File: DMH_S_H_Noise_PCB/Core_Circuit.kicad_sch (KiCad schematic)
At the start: 61 parts, among them Q1 BC548, Q2 MMBFJ113, Q3 BC548, SW1 SW_Push, U1 TL074, U2 TL072, U3 TL074

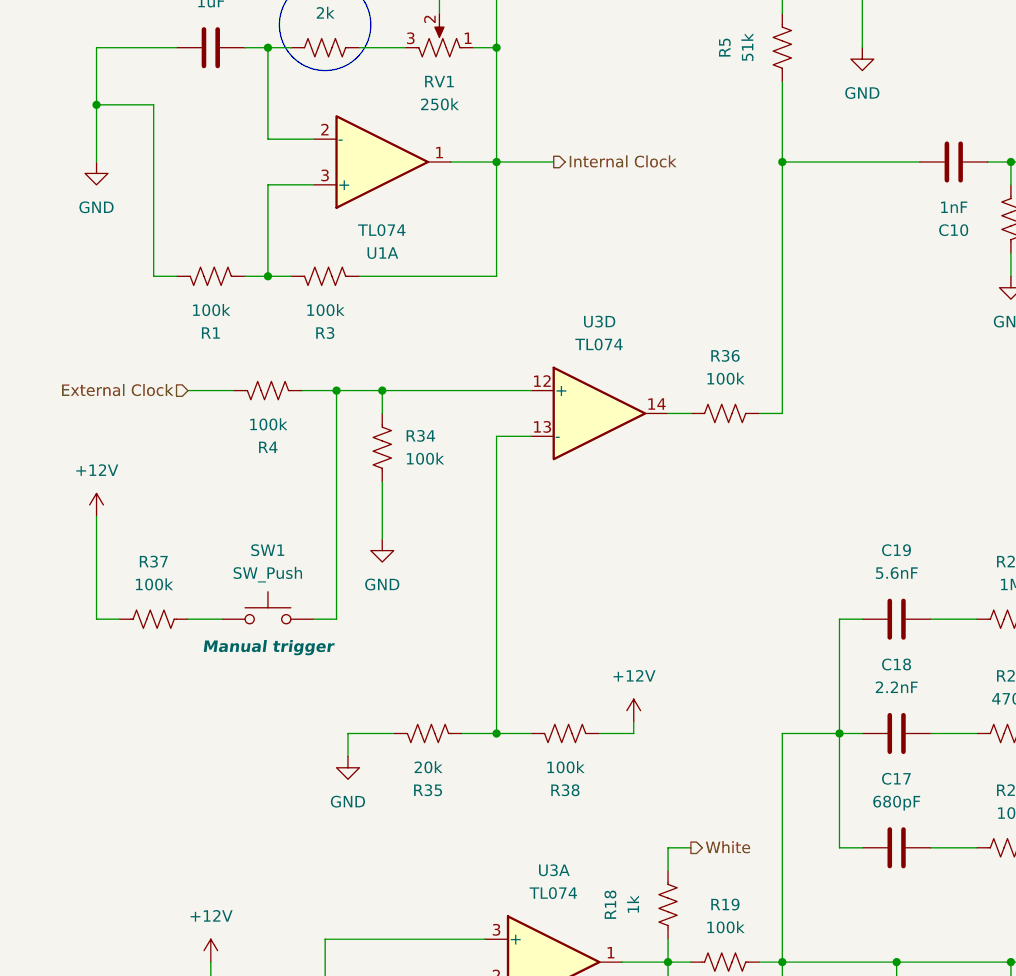
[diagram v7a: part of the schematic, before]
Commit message: Added toggle switch to schematic
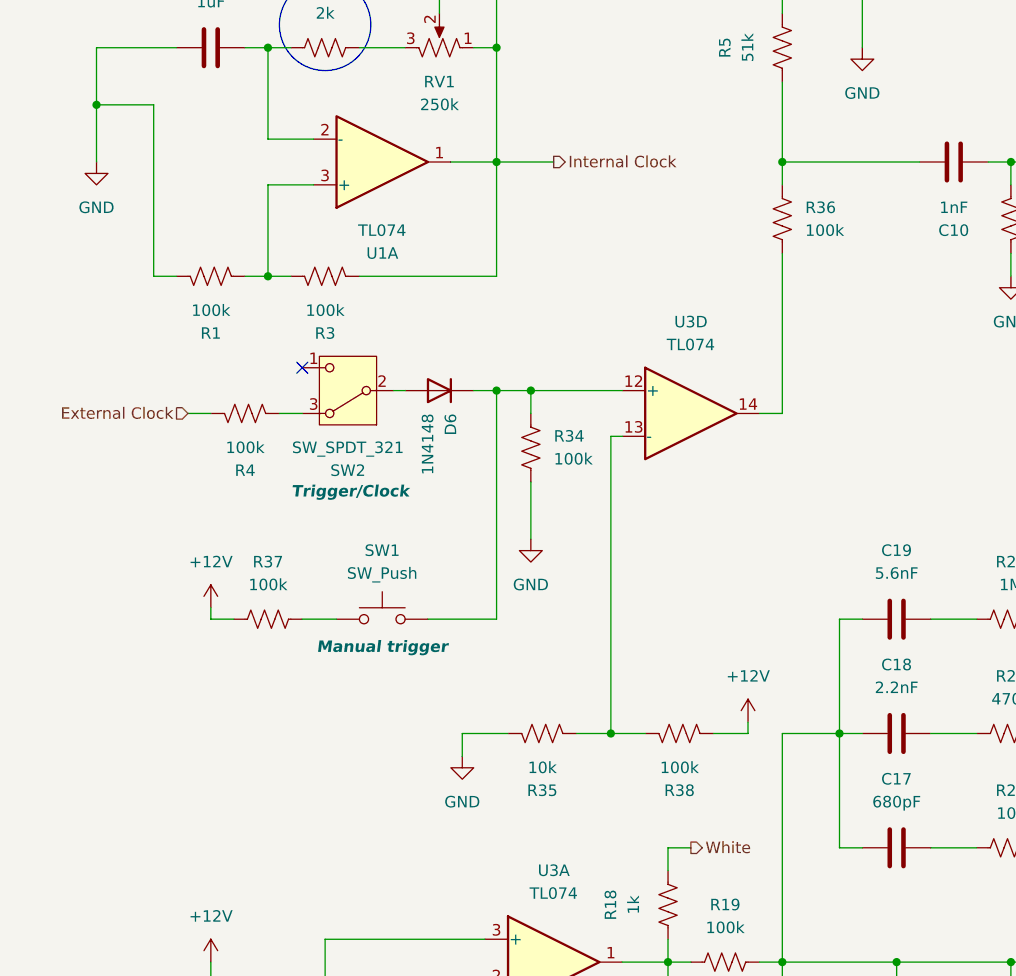
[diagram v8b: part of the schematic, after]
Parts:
- added D6: 1N4148, Diode_THT:D_DO-35_SOD27_P7.62mm_Horizontal, symbol Device:D
- added SW2: SW_SPDT_321, symbol Switch:SW_SPDT_321
- R35: value 20k -> 10k
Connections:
- net at R34.2, SW1.2, U3.12 (+): now also D6.1 (K); no longer R4.1
- new net: R4.1, SW2.3 (A)
- new net: D6.2 (A), SW2.2 (B)
- no-connect marks 1 -> 2
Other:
- moved on the sheet: R34, R35, R36, R37, R38, R4, SW1, U3D
